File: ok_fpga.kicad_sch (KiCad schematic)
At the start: 57 parts

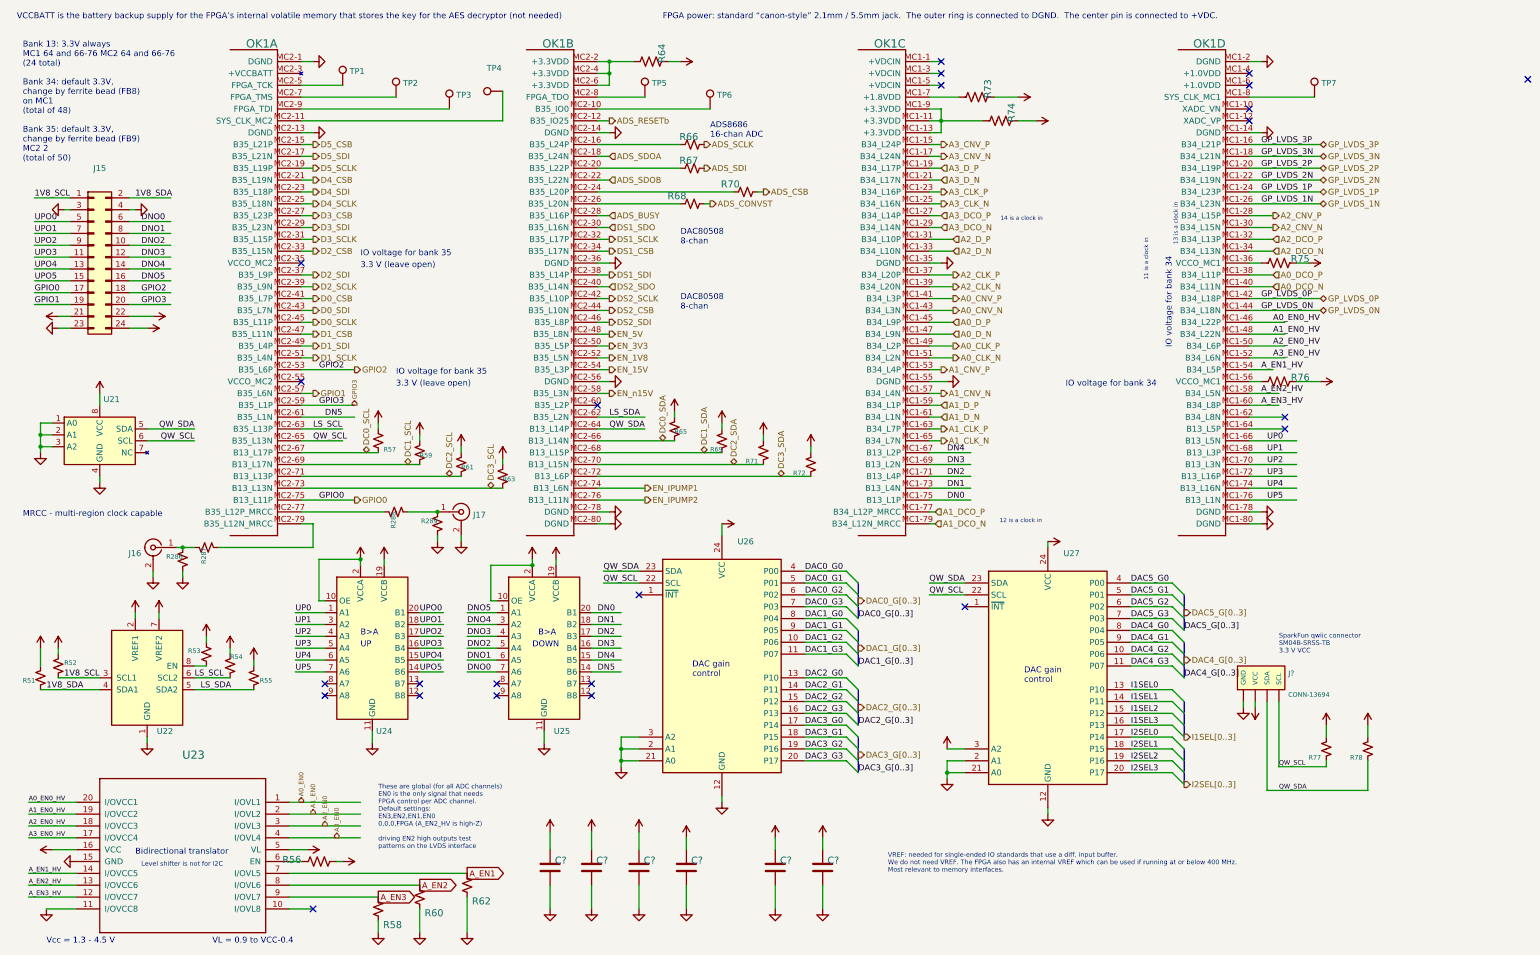
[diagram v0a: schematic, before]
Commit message: closes #31 - incorrect text on Howland current pump. Also, updated fast DAC symbol but not closing until layout is corrected
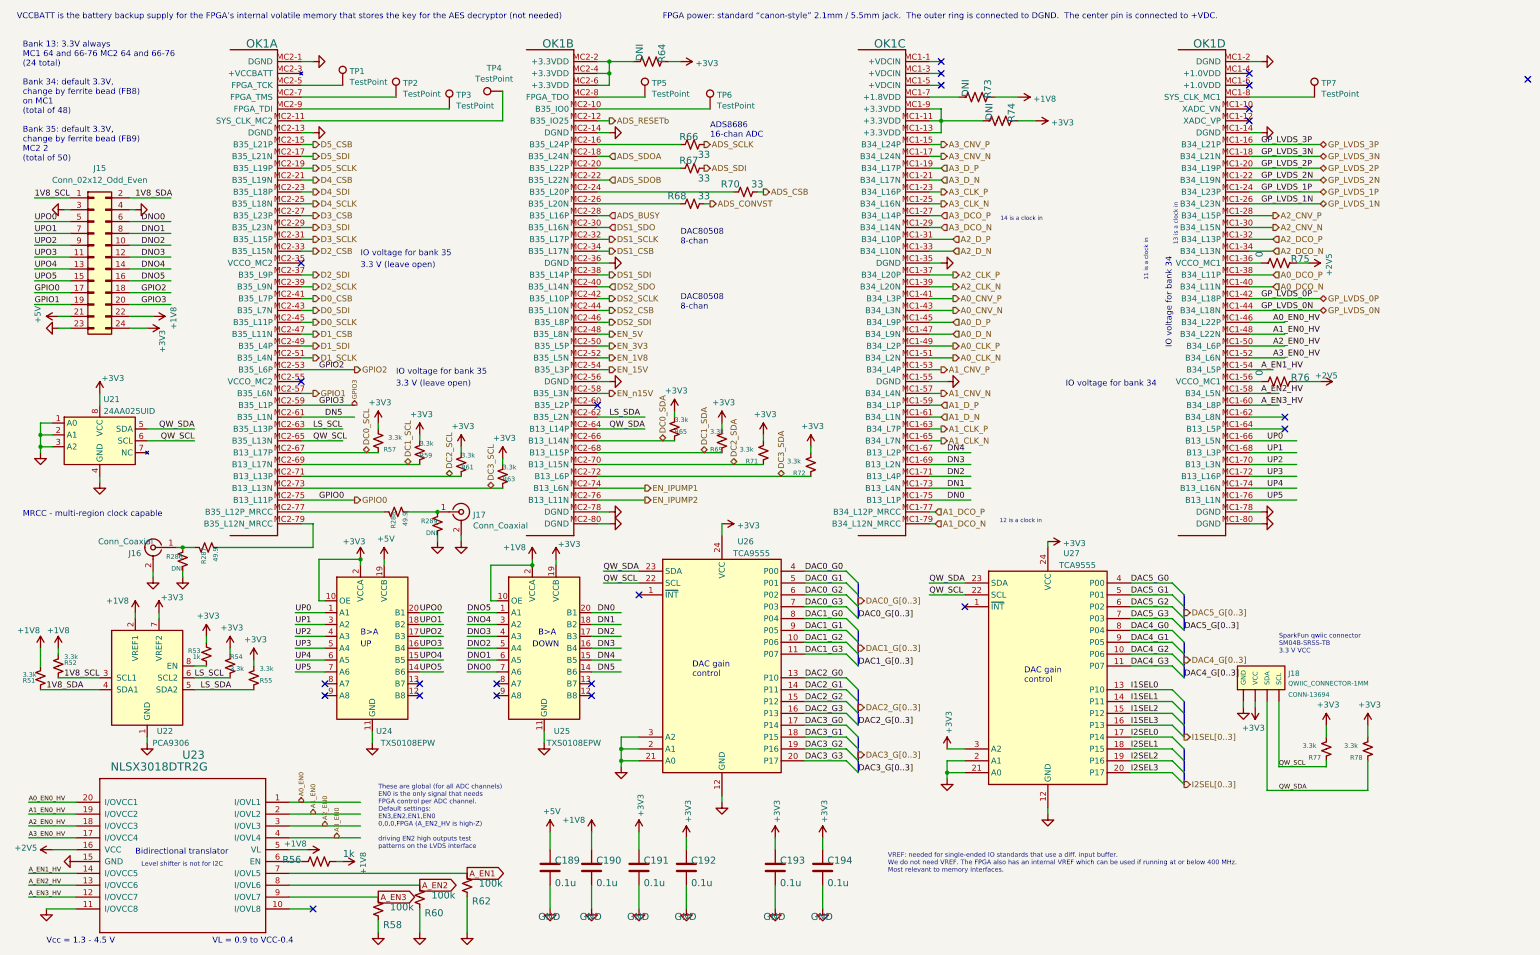
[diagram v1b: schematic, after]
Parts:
- C189, C190, C191, C192, C193, C194: renamed from C?; value (none) -> 0.1u; footprint (none) -> Capacitor_SMD:C_0603_1608Metric
- J15: value (none) -> Conn_02x12_Odd_Even; footprint (none) -> Connector_PinHeader_2.00mm:PinHeader_2x12_P2.00mm_Horizontal
- J16, J17: value (none) -> Conn_Coaxial; footprint (none) -> covg-kicad:BU-SMA-G
- J18: renamed from J?; value (none) -> QWIIC_CONNECTOR-1MM; footprint (none) -> Connectors:1X04_1MM_RA
- OK1: value (none) -> OPALKELLY_XEM7310; footprint (none) -> covg-kicad:OPALKELLY_XEM7310
- R286, R289, R64, R73, R74: value (none) -> DNI; footprint (none) -> Resistor_SMD:R_0603_1608Metric
- R287, R288: value (none) -> 49.9; footprint (none) -> Resistor_SMD:R_0603_1608Metric
- R51, R52, R54, R55, R57, R59, R61, R63, R65, R69, R71, R72, R77, R78: value (none) -> 3.3k; footprint (none) -> Resistor_SMD:R_0603_1608Metric
- R53, R56: value (none) -> 1k; footprint (none) -> Resistor_SMD:R_0603_1608Metric
- R58, R60, R62: value (none) -> 100k; footprint (none) -> Resistor_SMD:R_0603_1608Metric
- R66, R67, R68, R70: value (none) -> 33; footprint (none) -> Resistor_SMD:R_0603_1608Metric
- R75, R76: value (none) -> 0; footprint (none) -> Resistor_SMD:R_0603_1608Metric
- TP1, TP2, TP3, TP4, TP5, TP6, TP7: value (none) -> TestPoint; footprint (none) -> TestPoint:TestPoint_THTPad_1.5x1.5mm_Drill0.7mm
- U21: value (none) -> 24AA025UID; footprint (none) -> Package_SO:SOIC-8_3.9x4.9mm_P1.27mm
- U22: value (none) -> PCA9306; footprint (none) -> Package_SO:TSSOP-8_4.4x3mm_P0.65mm
- U23: value (none) -> NLSX3018DTR2G; footprint (none) -> Package_SO:TSSOP-20_4.4x6.5mm_P0.65mm
- U24, U25: value (none) -> TXS0108EPW; footprint (none) -> Package_SO:TSSOP-20_4.4x6.5mm_P0.65mm
- U26, U27: value (none) -> TCA9555; footprint (none) -> Package_SO:SSOP-24_5.3x8.2mm_P0.65mm
